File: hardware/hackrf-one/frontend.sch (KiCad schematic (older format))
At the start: 133 parts, among them J2 RF-SHIELD-FRAME, J3 RF-SHIELD-COVER, P13 GPO1, P17 GPO6, P19 GPO3, P21 REF_IN, P27 MIXER_SDATA, P31 MIXER_SCLK, P32 MIXER_ENX, P33 MIXER_RESETX, P34 MIX_BYPASS, P35 !MIX_BYPASS, P4 ANTENNA, P42 TX, P43 RX, P44 HP, P45 LP, P46 TX_MIX_BP, P47 RX_MIX_BP, P48 TX_AMP, P49 RX_AMP, P50 AMP_BYPASS, P51 !TX_AMP_PWR, P52 !RX_AMP_PWR, P6 GPO4, P7 GPO2, Q1 MOSFET_P, Q2 MOSFET_P, T1 MIX_IN_BALUN, T2 MIX_OUT_BALUN, U1 SKY13350, U10 SKY13350, U11 SKY13350, U12 SKY13317, U13 MGA-81563, U14 SKY13317, U2 SKY13350, U25 MGA-81563, U3 RX_LOWPASS_FILTER, U4 RFFC5072, U5 SKY13350, U6 SKY13350, U7 SKY13350, U8 RX_HIGHPASS_FILTER, U9 SKY13317

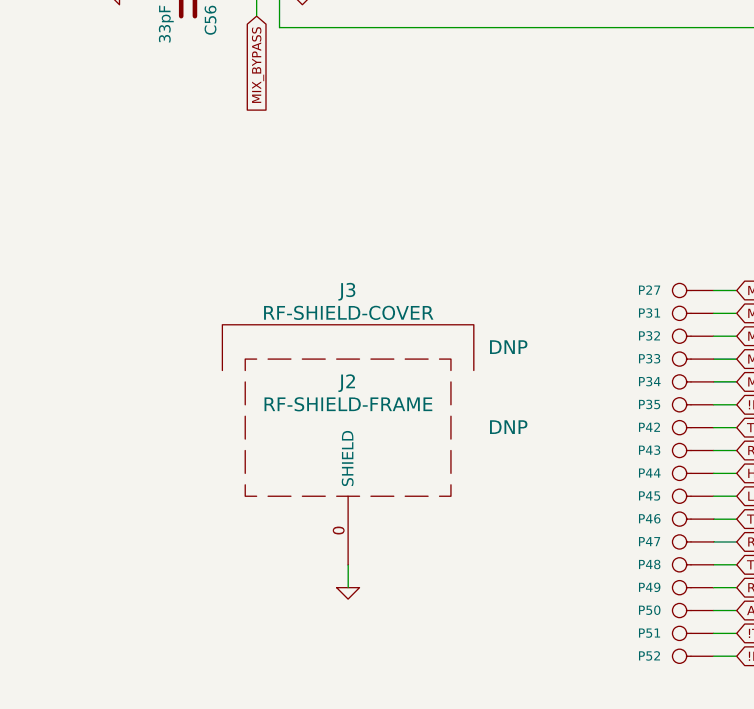
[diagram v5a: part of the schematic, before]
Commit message: exposed GND through mounting holes
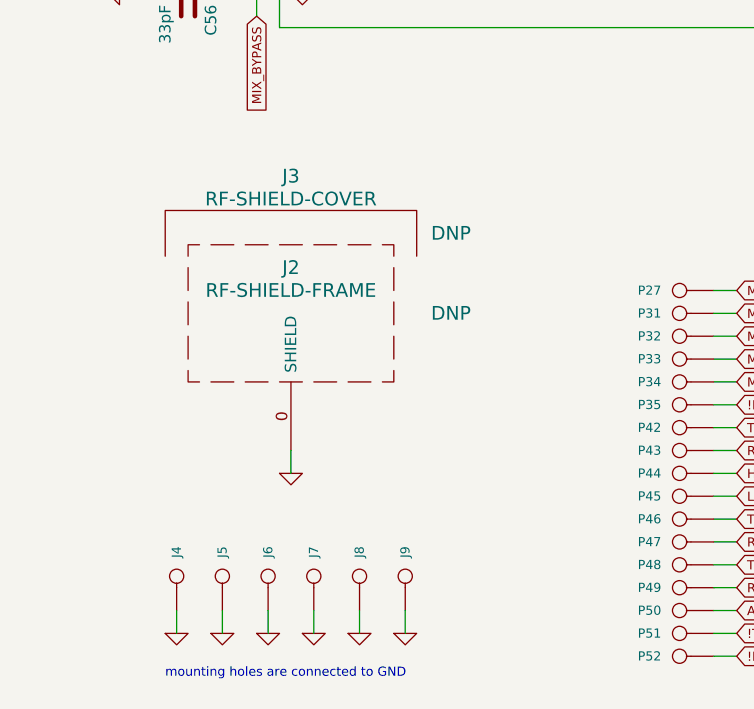
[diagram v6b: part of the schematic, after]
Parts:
- added J4, J5, J6, J7, J8, J9: MOUNTING_HOLE, symbol CONN_1
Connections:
- net GND: now also J4.1, J5.1, J6.1, J7.1, J8.1, J9.1
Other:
- note added: "mounting holes are connected to GND"
- moved on the sheet: J2, J3
